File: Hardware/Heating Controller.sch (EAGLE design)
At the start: 4 parts

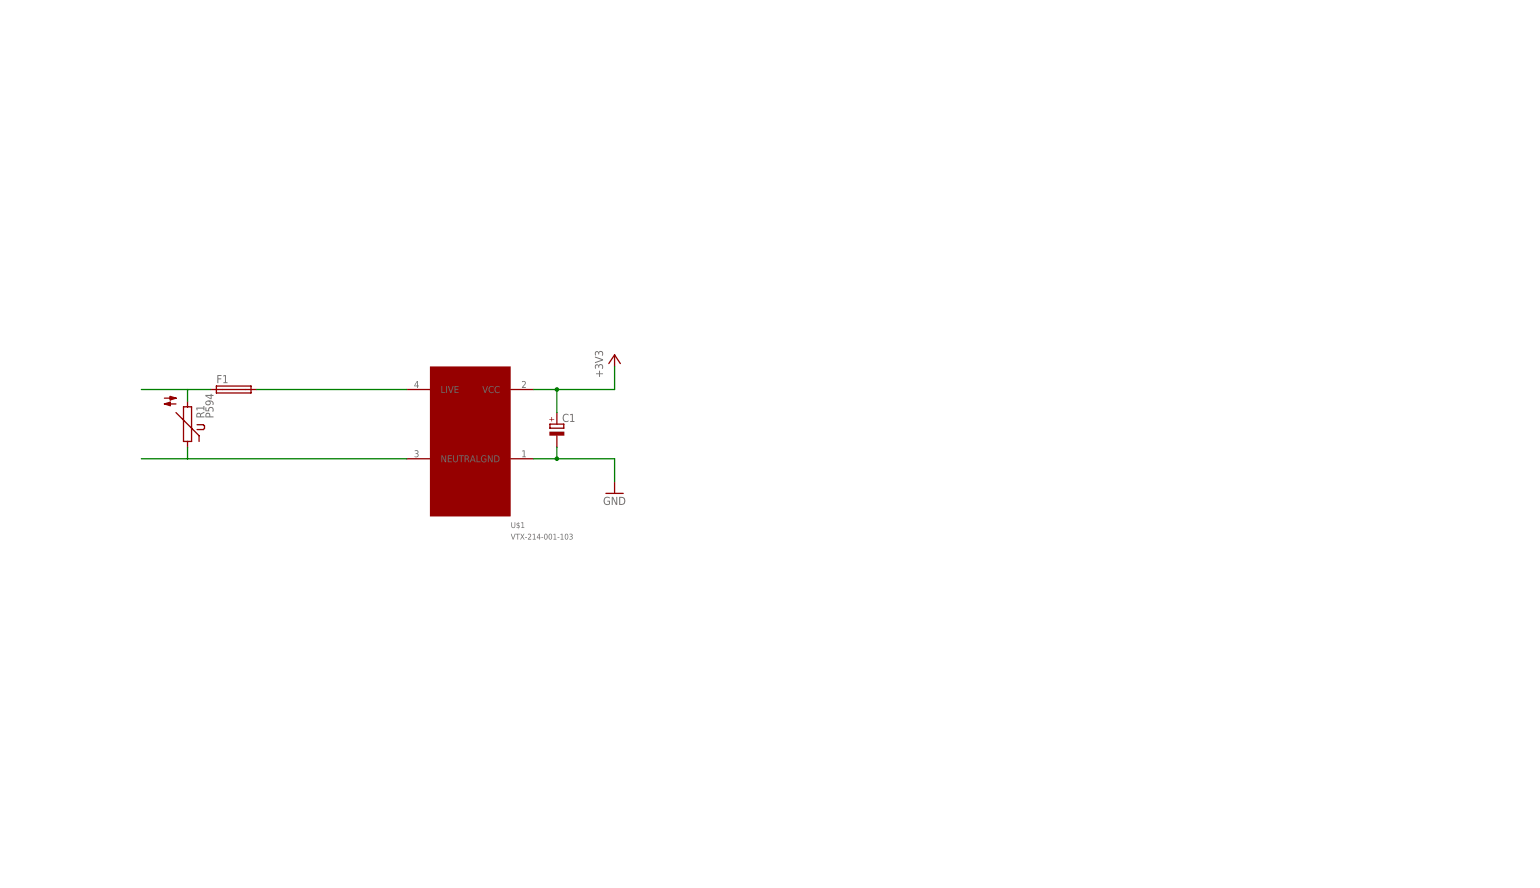
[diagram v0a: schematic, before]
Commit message: initial mockup of heating controller
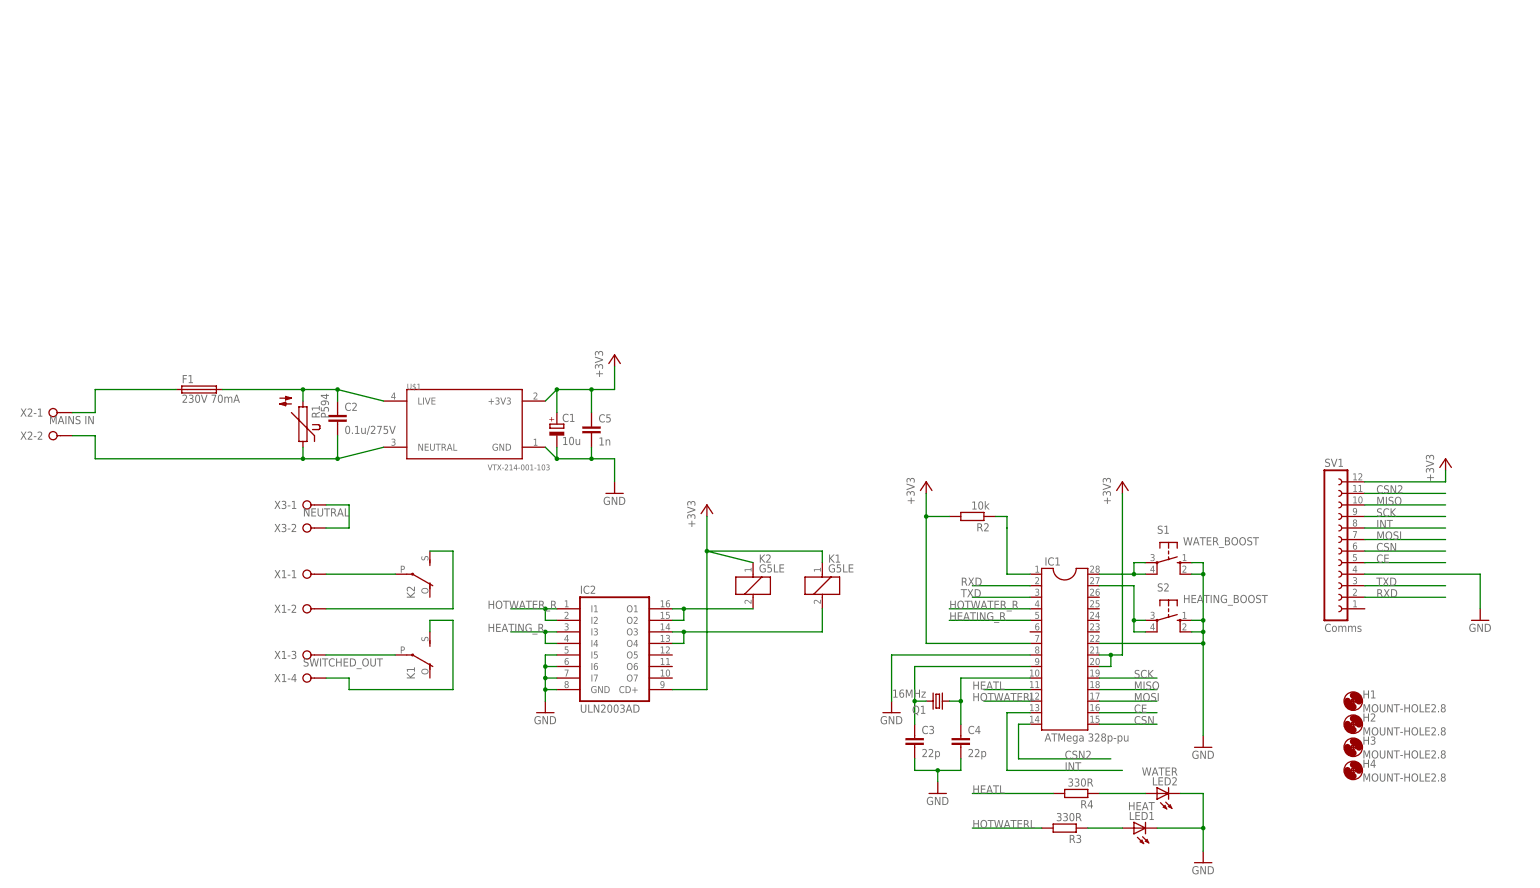
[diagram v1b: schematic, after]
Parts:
- added C2: 0.1u/275V, rcl:C-EU025-025X050
- added C3, C4: 22p, rcl:C-EUC1206K
- added C5: 1n, rcl:C-EUC1206K
- added H1, H2, H3, H4: MOUNT-HOLE2.8, holes:MOUNT-HOLE2.8
- added IC1: ATMega 328p-pu, ic-package:DIL28-4
- added IC2: ULN2003AD, uln-udn:ULN2003AD
- added K1, K2: G5LE, relay:G5LE
- added LED1: HEAT, led:LED5MM
- added LED2: WATER, led:LED5MM
- added Q1: 16MHz, crystal:CRYSTALHC49S
- added R2: 10k, rcl:R-EU_R1206W
- added R3, R4: 330R, rcl:R-EU_R1206W
- added S1: WATER_BOOST, switch-omron:40-XX
- added S2: HEATING_BOOST, switch-omron:40-XX
- added SV1: Comms, con-lsta:FE12W
- added X1: SWITCHED_OUT, con-wago-508:W237-04P
- added X2: MAINS IN, con-wago-508:W237-02P
- added X3: NEUTRAL, con-wago-508:W237-02P
- C1: value (none) -> 10u
- F1: value (none) -> 230V 70mA
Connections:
- new net CE: IC1.16, SV1.5
- new net CSN: IC1.15, SV1.6
- new net CSN2: IC1.14, SV1.11
- new net HEATING_R: IC1.5, IC2.I3, IC2.I4
- new net HEATL: IC1.11, R4.2
- new net HOTWATERL: IC1.12, R3.2
- new net HOTWATER_R: IC1.4, IC2.I1, IC2.I2
- new net INT: IC1.13, SV1.8
- new net MISO: IC1.18, SV1.10
- new net MOSI: IC1.17, SV1.7
- new net N$10: IC1.27, S2.P, S2.P1
- new net N$12: IC2.O1, IC2.O2, K21.2
- new net N$13: IC2.O3, IC2.O4, K11.2
- new net N$15: K22.P, X1-1.KL
- new net N$16: K22.S, X1-2.KL
- new net N$17: K12.P, X1-3.KL
- new net N$18: K12.S, X1-4.KL
- new net N$19: X3-1.KL, X3-2.KL
- new net N$4: IC1.1, R2.1
- new net N$5: C3.1, IC1.9, Q1.2
- new net N$6: C4.1, IC1.10, Q1.1
- new net N$7: LED1.A, R3.1
- new net N$8: LED2.A, R4.1
- new net N$9: IC1.28, S1.P, S1.P1
- new net RXD: IC1.2, SV1.2
- new net SCK: IC1.19, SV1.9
- new net TXD: IC1.3, SV1.3
- net +3V3: now also C5.1, IC1.20, IC1.21, IC1.7, IC2.CD+, K11.1, K21.1, R2.2, SV1.12, U$1.+3V3; no longer U$1.VCC
- net GND: now also C3.2, C4.2, C5.2, IC1.22, IC1.8, IC2.GND, IC2.I5, IC2.I6, IC2.I7, LED1.C, LED2.C, S1.S, S1.S1, S2.S, S2.S1, SV1.4
- net N$1: now also X2-1.KL; no longer R1.2
- net N$2: now also C2.1, R1.2
- net N$3: now also C2.2, X2-2.KL
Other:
- moved on the sheet: F1, R1

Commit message: added optocoupled output to add extra layer of isolation
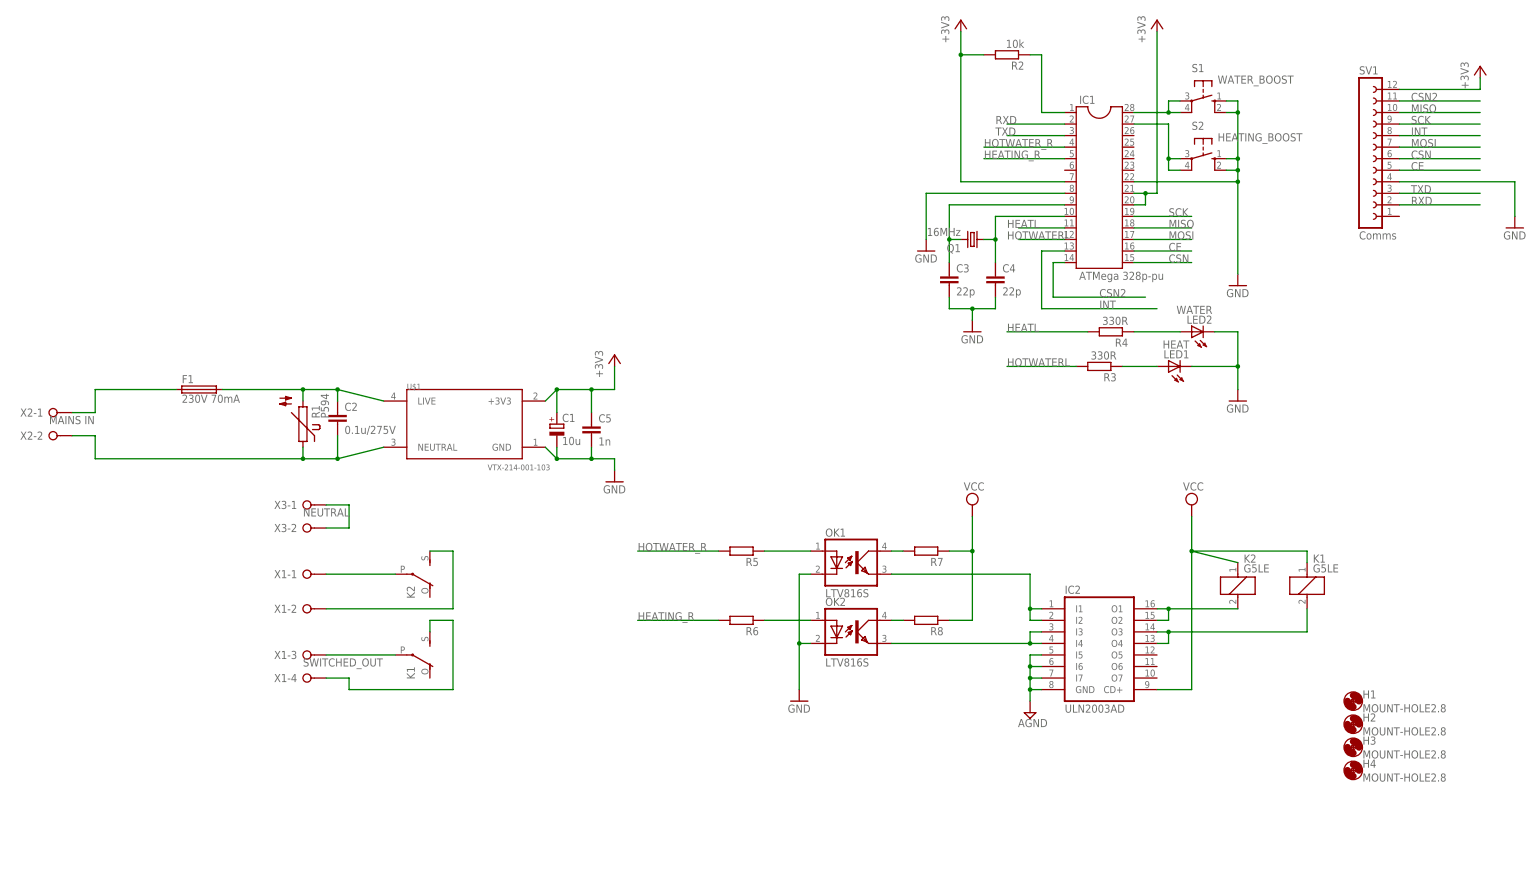
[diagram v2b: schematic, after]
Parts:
- added OK1, OK2: LTV816S, optocoupler:LTV816S
- added R5, R6, R7, R8: (no value), rcl:R-EU_R1206W
- C2: device rcl:C-EU025-025X050 -> rcl:C-EUC1206K
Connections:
- new net AGND: IC2.GND, IC2.I5, IC2.I6, IC2.I7
- new net N$11: OK1.A, R5.1
- new net N$14: OK2.A, R6.1
- new net N$20: OK1.COL, R7.2
- new net N$21: OK2.COL, R8.2
- new net N$22: IC2.I1, IC2.I2, OK1.EMIT
- new net N$23: IC2.I3, IC2.I4, OK2.EMIT
- new net VCC: IC2.CD+, K11.1, K21.1, R7.1, R8.1
- net +3V3: no longer IC2.CD+, K11.1, K21.1
- net GND: now also OK1.C, OK2.C; no longer IC2.GND, IC2.I5, IC2.I6, IC2.I7
- net HEATING_R: now also R6.2; no longer IC2.I3, IC2.I4
- net HOTWATER_R: now also R5.2; no longer IC2.I1, IC2.I2
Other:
- moved on the sheet: C3, C4, IC1, IC2, K1, K2, LED1, LED2, Q1, R2, R3, R4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

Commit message: Updated wrong fuse holder and processor footprint
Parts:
- F1: device fuse:GSH15 -> fuse:SH22,5A
- IC1: device ic-package:DIL28-4 -> ic-package:DIL28-3
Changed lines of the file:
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@@
 <parts>
 <part name="U$1" library="VTX214001103" deviceset="VTX-214-001-103" device=""/>
-<part name="F1" library="fuse" deviceset="GSH15" device="" value="230V 70mA"/>
+<part name="F1" library="fuse" deviceset="SH22,5A" device="" value="230V 70mA"/>
 <part name="R1" library="varistor" deviceset="P594" device=""/>
 <part name="C1" library="rcl" deviceset="CPOL-EU" device="153CLV-1010" value="10u"/>
@@
 <part name="LED1" library="led" deviceset="LED" device="5MM" value="HEAT"/>
 <part name="LED2" library="led" deviceset="LED" device="5MM" value="WATER"/>
-<part name="IC1" library="ic-package" deviceset="DIL28" device="-4" value="ATMega 328p-pu"/>
+<part name="IC1" library="ic-package" deviceset="DIL28" device="-3" value="ATMega 328p-pu"/>
 <part name="Q1" library="crystal" deviceset="CRYSTAL" device="HC49S" value="16MHz"/>
 <part name="R2" library="rcl" deviceset="R-EU_" device="R1206W" value="10k"/>

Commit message: Inital Mockup of board component placement
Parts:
- added L1, L2: (no value), rcl:L-EUL1812
- C1: value 10u -> 47u; device rcl:CPOL-EU153CLV-1010 -> resistor:CPOL-EUE2.5-7
- C2: device rcl:C-EUC1206K -> capacitor-wima:C15/5
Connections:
- removed net AGND: IC2.GND, IC2.I5, IC2.I6, IC2.I7
- new net +3V3A: L1.1, U$1.+3V3
- net +3V3: now also L1.2, L2.1; no longer U$1.+3V3
- net GND: now also IC2.GND, IC2.I5, IC2.I6, IC2.I7
- net N$1: now also X2-2.KL; no longer X2-1.KL
- net N$15: now also X1-2.KL; no longer X1-1.KL
- net N$16: now also X1-1.KL; no longer X1-2.KL
- net N$17: now also X1-4.KL; no longer X1-3.KL
- net N$18: now also X1-3.KL; no longer X1-4.KL
- net N$3: now also X2-1.KL; no longer X2-2.KL
- net VCC: now also L2.2
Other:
- moved on the sheet: C1, C5, X1-1, X1-2, X1-3, X1-4, X2-1, X2-2

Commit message: fixed incorrect resistor footprints. Added AGND Isolation Inductor. Added Silk Text. Moved Component Labels
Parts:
- added L3: (no value), rcl:L-EUL3230M
- L1, L2: device rcl:L-EUL1812 -> rcl:L-EUL3230M
- R2, R3, R4, R5, R6, R7, R8: device rcl:R-EU_R1206W -> rcl:R-EU_R1206
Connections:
- new net AGND: IC2.GND, IC2.I5, IC2.I6, IC2.I7, L3.2
- net GND: now also L3.1; no longer IC2.GND, IC2.I5, IC2.I6, IC2.I7
